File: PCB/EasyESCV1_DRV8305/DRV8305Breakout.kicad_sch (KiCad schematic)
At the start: 39 parts, among them Q1 CSD16556Q5B, Q2 CSD16556Q5B, Q3 CSD16556Q5B, Q4 CSD16556Q5B, Q5 CSD16556Q5B, Q6 CSD16556Q5B, U1 DRV83053PHP, U3 TPD4E05U06DQAR

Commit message: Finished REV1 Schematic Awaiting Review
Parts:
- C10, C11, C12: value 0.1U -> 0.1u
- renumbered TP1 to PA, TP2 to PB, TP3 to PC
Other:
- note added: "ESD Protection"
- note added: "Motor Driver"
- note added: "Output Phase A"
- note added: "Output Phase B"
- note added: "Output Phase C"
- company: (none) -> Buckley Boards 
- title: (none) -> Easy ESC
- moved on the sheet: C1, C10, C11, C12, C13, C14, C15, C16, C17, C2, C3, C4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

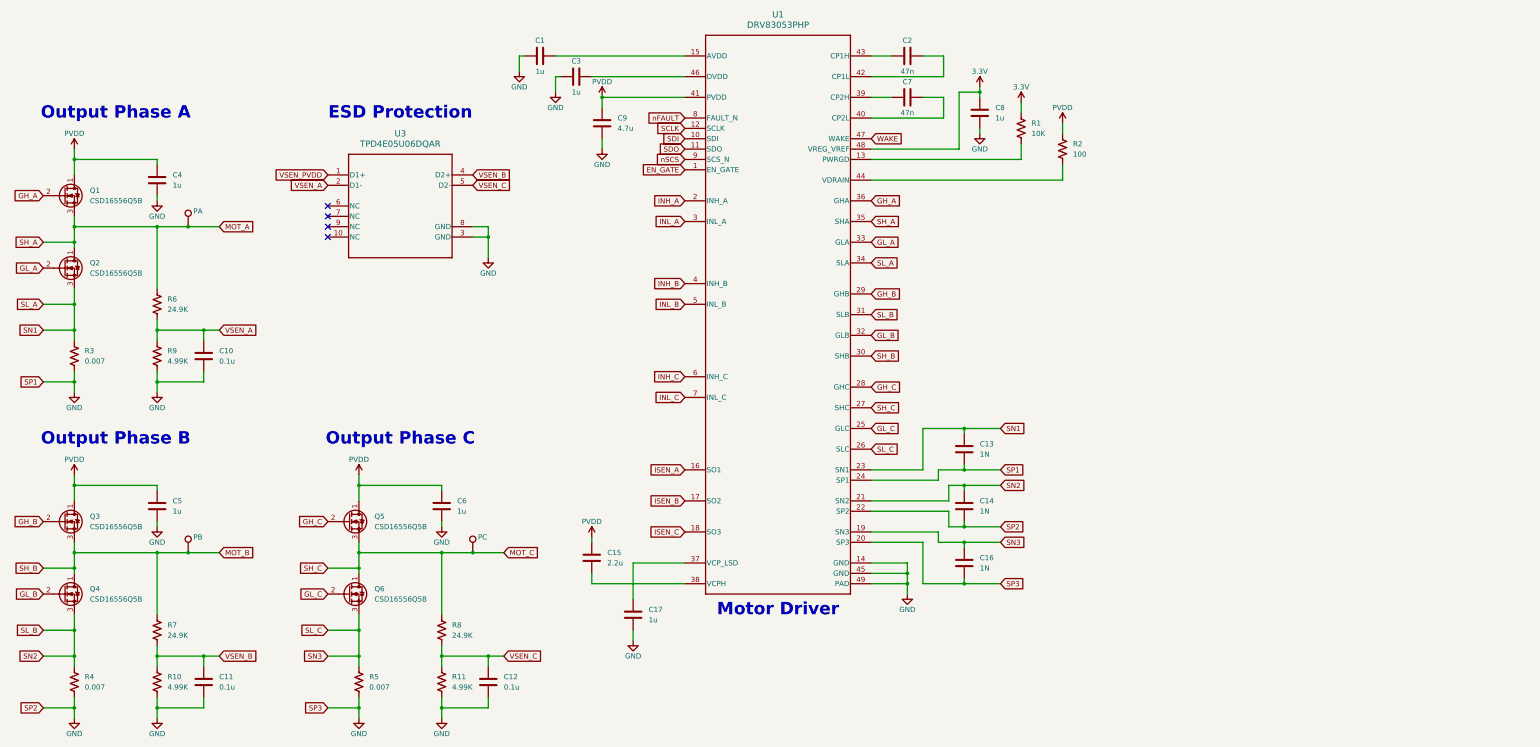
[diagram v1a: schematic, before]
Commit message: Fixed issue with fet symbol and started layout
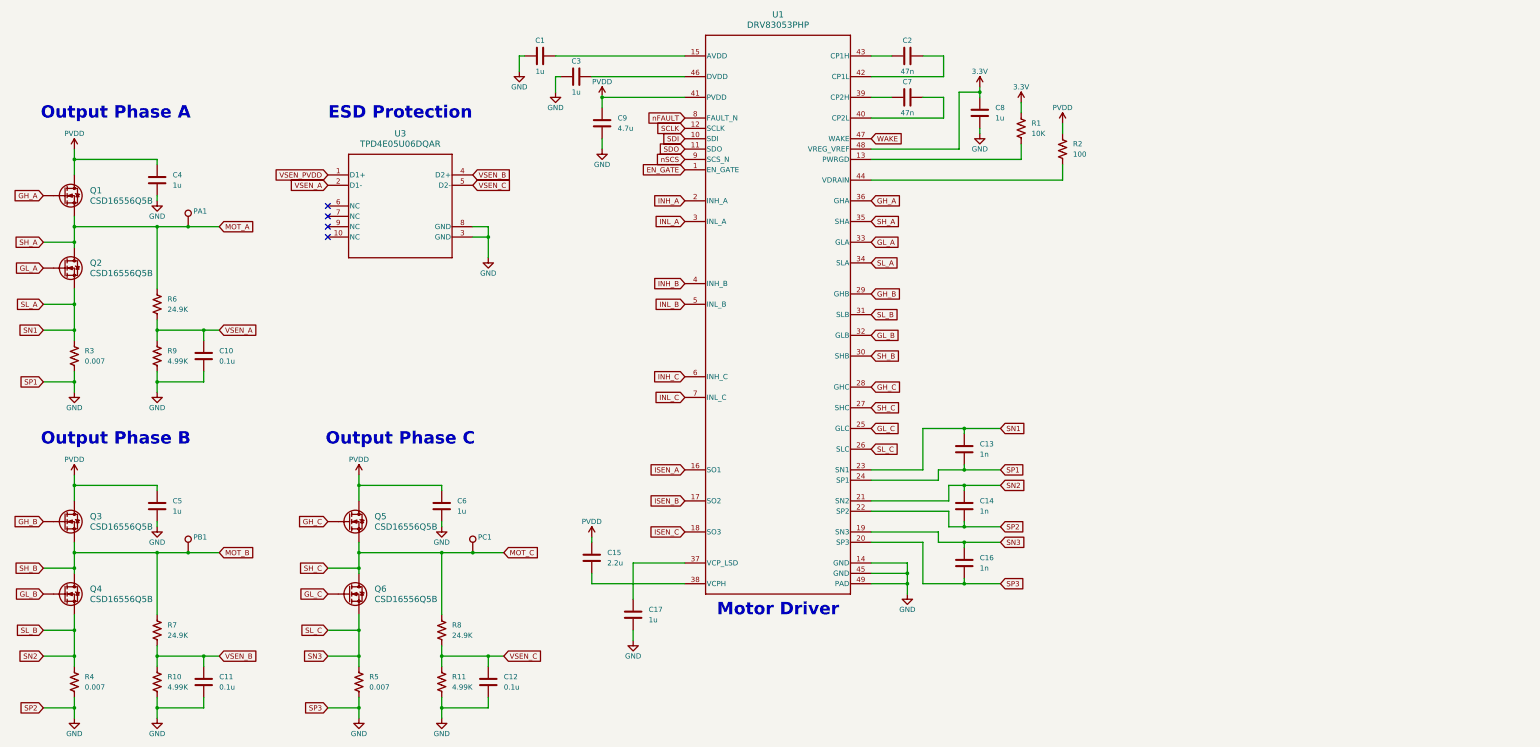
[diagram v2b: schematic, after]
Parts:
- removed Q1, Q2, Q3, Q4, Q5, Q6: CSD16556Q5B, CSD16556Q5B:DNK0008A, symbol Device:Q_NMOS_DGS
- added Q1, Q2, Q3, Q4, Q5, Q6: CSD16556Q5B, CSD16556Q5B:DNK0008A, symbol CSD16556Q5B:CSD16556Q5B
- C1, C15, C17, C2, C3, C4, C5, C6, C7, C8, C9: footprint (none) -> Capacitor_SMD:C_0603_1608Metric
- C10, C11, C12: footprint (none) -> Capacitor_SMD:C_0402_1005Metric
- C13, C14, C16: value 1N -> 1n; footprint (none) -> Capacitor_SMD:C_0402_1005Metric
- PA1: renamed from PA; footprint (none) -> TestPoint:TestPoint_Pad_D3.0mm
- PB1: renamed from PB; footprint (none) -> TestPoint:TestPoint_Pad_D3.0mm
- PC1: renamed from PC; footprint (none) -> TestPoint:TestPoint_Pad_D3.0mm
- R1, R2: footprint (none) -> Fuse:Fuse_0603_1608Metric
- R10, R11, R9: footprint (none) -> Resistor_SMD:R_0402_1005Metric
- R3, R4, R5: footprint (none) -> Resistor_SMD:R_2512_6332Metric
- R6, R7, R8: footprint (none) -> Resistor_SMD:R_0603_1608Metric
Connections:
- net GH_A: now also Q1.4 (G)
- net GH_B: now also Q3.4 (G)
- net GH_C: now also Q5.4 (G)
- net GL_A: now also Q2.4 (G)
- net GL_B: now also Q4.4 (G)
- net GL_C: now also Q6.4 (G)
- net MOT_A: now also Q1.1 (S), Q1.2 (S), Q1.3 (S), Q2.5 (D), Q2.6 (D), Q2.7 (D), Q2.8 (D)
- net MOT_B: now also Q3.1 (S), Q3.2 (S), Q3.3 (S), Q4.5 (D), Q4.6 (D), Q4.7 (D), Q4.8 (D)
- net MOT_C: now also Q5.1 (S), Q5.2 (S), Q5.3 (S), Q6.5 (D), Q6.6 (D), Q6.7 (D), Q6.8 (D)
- net PVDD: now also Q1.5 (D), Q1.6 (D), Q1.7 (D), Q1.8 (D), Q3.5 (D), Q3.6 (D), Q3.7 (D), Q3.8 (D), Q5.5 (D), Q5.6 (D), Q5.7 (D), Q5.8 (D)
- net SL_A: now also Q2.1 (S), Q2.2 (S), Q2.3 (S)
- net SL_B: now also Q4.1 (S), Q4.2 (S), Q4.3 (S)
- net SL_C: now also Q6.1 (S), Q6.2 (S), Q6.3 (S)

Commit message: Started Layout
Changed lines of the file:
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@@
 	)
 	(junction
-		(at 34.29 184.15)
+		(at 256.54 33.02)
 		(diameter 0)
 		(color 0 0 0 0)
 	)
 	(junction
-		(at 256.54 33.02)
+		(at 273.05 139.7)
 		(diameter 0)
 		(color 0 0 0 0)
@@
 	)
 	(junction
-		(at 34.29 49.53)
+		(at 273.05 153.67)
 		(diameter 0)
 		(color 0 0 0 0)
 	)
 	(junction
-		(at 34.29 104.14)
+		(at 34.29 49.53)
 		(diameter 0)
 		(color 0 0 0 0)
@@
 	)
 	(junction
-		(at 104.14 184.15)
-		(diameter 0)
-		(color 0 0 0 0)
-	)
-	(junction
 		(at 163.83 34.29)
 		(diameter 0)
@@
 	(wire
 		(pts
-			(xy 96.52 184.15) (xy 104.14 184.15)
-		)
-		(stroke
-			(width 0)
-			(type default)
-		)
-	)
-	(wire
-		(pts
 			(xy 54.61 66.04) (xy 62.23 66.04)
 		)
@@
 	(wire
 		(pts
-			(xy 26.67 184.15) (xy 34.29 184.15)
-		)
-		(stroke
-			(width 0)
-			(type default)
-		)
-	)
-	(wire
-		(pts
 			(xy 104.14 146.05) (xy 124.46 146.05)
 		)
@@
 	(wire
 		(pts
-			(xy 34.29 184.15) (xy 34.29 186.69)
+			(xy 34.29 181.61) (xy 34.29 186.69)
 		)
 		(stroke
@@
 	(wire
 		(pts
-			(xy 34.29 104.14) (xy 34.29 106.68)
-		)
-		(stroke
-			(width 0)
-			(type default)
-		)
-	)
-	(wire
-		(pts
 			(xy 104.14 129.54) (xy 124.46 129.54)
 		)
@@
 	(wire
 		(pts
-			(xy 252.73 139.7) (xy 261.62 139.7)
+			(xy 252.73 139.7) (xy 273.05 139.7)
 		)
 		(stroke
@@
 	(wire
 		(pts
-			(xy 152.4 29.21) (xy 153.67 29.21)
+			(xy 273.05 153.67) (xy 273.05 156.21)
 		)
 		(stroke
@@
 	(wire
 		(pts
-			(xy 66.04 91.44) (xy 54.61 91.44)
+			(xy 152.4 29.21) (xy 153.67 29.21)
 		)
 		(stroke
@@
 	(wire
 		(pts
-			(xy 276.86 40.64) (xy 276.86 43.18)
+			(xy 66.04 91.44) (xy 54.61 91.44)
 		)
 		(stroke
@@
 	(wire
 		(pts
-			(xy 252.73 139.7) (xy 252.73 138.43)
+			(xy 276.86 40.64) (xy 276.86 43.18)
 		)
 		(stroke
@@
 	(wire
 		(pts
-			(xy 252.73 125.73) (xy 261.62 125.73)
+			(xy 252.73 139.7) (xy 252.73 138.43)
 		)
 		(stroke
@@
 	(wire
 		(pts
-			(xy 54.61 171.45) (xy 54.61 168.91)
+			(xy 252.73 125.73) (xy 273.05 125.73)
 		)
 		(stroke
@@
 	(wire
 		(pts
-			(xy 242.57 153.67) (xy 242.57 143.51)
+			(xy 54.61 171.45) (xy 54.61 168.91)
 		)
 		(stroke
@@
 	(wire
 		(pts
-			(xy 62.23 66.04) (xy 69.85 66.04)
+			(xy 242.57 153.67) (xy 242.57 143.51)
 		)
 		(stroke
@@
 	(wire
 		(pts
-			(xy 135.89 171.45) (xy 124.46 171.45)
+			(xy 62.23 66.04) (xy 69.85 66.04)
 		)
 		(stroke
@@
 	(wire
 		(pts
-			(xy 104.14 184.15) (xy 104.14 186.69)
+			(xy 135.89 171.45) (xy 124.46 171.45)
 		)
 		(stroke
@@
 	(wire
 		(pts
-			(xy 34.29 104.14) (xy 34.29 101.6)
+			(xy 34.29 101.6) (xy 34.29 106.68)
 		)
 		(stroke
@@
 	(wire
 		(pts
-			(xy 26.67 104.14) (xy 34.29 104.14)
-		)
-		(stroke
-			(width 0)
-			(type default)
-		)
-	)
-	(wire
-		(pts
 			(xy 252.73 143.51) (xy 261.62 143.51)
 		)
@@
 	(wire
 		(pts
-			(xy 34.29 184.15) (xy 34.29 181.61)
-		)
-		(stroke
-			(width 0)
-			(type default)
-		)
-	)
-	(wire
-		(pts
-			(xy 252.73 153.67) (xy 261.62 153.67)
+			(xy 252.73 153.67) (xy 273.05 153.67)
 		)
 		(stroke
@@
 	(wire
 		(pts
-			(xy 104.14 184.15) (xy 104.14 181.61)
+			(xy 104.14 181.61) (xy 104.14 186.69)
 		)
 		(stroke
@@
 	(wire
 		(pts
+			(xy 273.05 153.67) (xy 273.05 139.7)
+		)
+		(stroke
+			(width 0)
+			(type default)
+		)
+	)
+	(wire
+		(pts
 			(xy 54.61 184.15) (xy 66.04 184.15)
 		)
@@
 	(wire
 		(pts
+			(xy 273.05 139.7) (xy 273.05 125.73)
+		)
+		(stroke
+			(width 0)
+			(type default)
+		)
+	)
+	(wire
+		(pts
 			(xy 66.04 171.45) (xy 66.04 173.99)
 		)
@@
 		)
 	)
-	(global_label "SP3"
-		(shape input)
-		(at 96.52 184.15 180)
-		(fields_autoplaced yes)
-		(effects
-			(font
-				(size 1.27 1.27)
-			)
-			(justify right)
-		)
-		(property "Intersheetrefs" "${INTERSHEET_REFS}"
-			(at 89.8458 184.15 0)
-			(effects
-				(font
-					(size 1.27 1.27)
-				)
-				(justify right)
-				(hide yes)
-			)
-		)
-	)
 	(global_label "INL_A"
 		(shape input)
@@
 		)
 	)
-	(global_label "SP3"
-		(shape input)
-		(at 261.62 153.67 0)
-		(fields_autoplaced yes)
-		(effects
-			(font
-				(size 1.27 1.27)
-			)
-			(justify left)
-		)
-		(property "Intersheetrefs" "${INTERSHEET_REFS}"
-			(at 268.2942 153.67 0)
-			(effects
-				(font
-					(size 1.27 1.27)
-				)
-				(justify left)
-				(hide yes)
-			)
-		)
-	)
 	(global_label "GH_C"
 		(shape input)
@@
 		)
 	)
-	(global_label "SP1"
-		(shape input)
-		(at 26.67 104.14 180)
-		(fields_autoplaced yes)
-		(effects
-			(font
-				(size 1.27 1.27)
-			)
-			(justify right)
-		)
-		(property "Intersheetrefs" "${INTERSHEET_REFS}"
-			(at 19.9958 104.14 0)
-			(effects
-				(font
-					(size 1.27 1.27)
-				)
-				(justify right)
-				(hide yes)
-			)
-		)
-	)
 	(global_label "VSEN_B"
 		(shape input)
@@
 		)
 	)
-	(global_label "SP2"
-		(shape input)
-		(at 261.62 139.7 0)
-		(fields_autoplaced yes)
-		(effects
-			(font
-				(size 1.27 1.27)
-			)
-			(justify left)
-		)
-		(property "Intersheetrefs" "${INTERSHEET_REFS}"
-			(at 268.2942 139.7 0)
-			(effects
-				(font
-					(size 1.27 1.27)
-				)
-				(justify left)
-				(hide yes)
-			)
-		)
-	)
 	(global_label "MOT_C"
 		(shape input)
@@
 		)
 	)
-	(global_label "SP2"
-		(shape input)
-		(at 26.67 184.15 180)
-		(fields_autoplaced yes)
-		(effects
-			(font
-				(size 1.27 1.27)
-			)
-			(justify right)
-		)
-		(property "Intersheetrefs" "${INTERSHEET_REFS}"
-			(at 19.9958 184.15 0)
-			(effects
-				(font
-					(size 1.27 1.27)
-				)
-				(justify right)
-				(hide yes)
-			)
-		)
-	)
 	(global_label "GL_C"
 		(shape input)
@@
 		)
 	)
-	(global_label "SP1"
-		(shape input)
-		(at 261.62 125.73 0)
-		(fields_autoplaced yes)
-		(effects
-			(font
-				(size 1.27 1.27)
-			)
-			(justify left)
-		)
-		(property "Intersheetrefs" "${INTERSHEET_REFS}"
-			(at 268.2942 125.73 0)
-			(effects
-				(font
-					(size 1.27 1.27)
-				)
-				(justify left)
-				(hide yes)
-			)
-		)
-	)
 	(global_label "GH_A"
 		(shape input)
@@
 					(unit 1)
 				)
+			)
+		)
+	)
+	(symbol
+		(lib_id "power:GND")
+		(at 273.05 156.21 0)
+		(unit 1)
+		(exclude_from_sim no)
+		(in_bom yes)
+		(on_board yes)
+		(dnp no)
+		(property "Reference" "#PWR056"
+			(at 273.05 162.56 0)
+			(effects
+				(font
+					(size 1.27 1.27)
+				)
+				(hide yes)
+			)
+		)
+		(property "Value" "GND"
+			(at 273.05 160.02 0)
+			(effects
+				(font
+					(size 1.27 1.27)
+				)
+			)
+		)
+		(property "Footprint" ""
+			(at 273.05 156.21 0)
+			(effects
+				(font
+					(size 1.27 1.27)
+				)
+				(hide yes)
+			)
+		)
+		(property "Datasheet" ""
+			(at 273.05 156.21 0)
+			(effects
+				(font
+					(size 1.27 1.27)
+				)
+				(hide yes)
+			)
+		)
+		(property "Description" "Power symbol creates a global label with name \"GND\" , ground"
+			(at 273.05 156.21 0)
+			(effects
+				(font
+					(size 1.27 1.27)
+				)
+				(hide yes)
+			)
+		)
+		(pin "1"
+		)
+		(instances
+			(project "EasyESCV1_DRV8305"
+				(path "/6c304649-7c80-4a4c-b925-07b9210ad53d/8a0cf24a-00c0-47a8-b582-1a7bbe5ca078"
+					(reference "#PWR056")
+					(unit 1)
+				)
